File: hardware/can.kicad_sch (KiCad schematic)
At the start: 8 parts, among them U6 ATA6561

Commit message: Assign footprints to symbols
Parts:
- FB1, FB2: value 60R@100MHz -> 50mΩ@100MHz; footprint Inductor_SMD:L_0603_1608Metric -> Inductor_SMD:L_1206_3216Metric
- JP1: footprint Connector_PinHeader_2.54mm:PinHeader_1x02_P2.54mm_Vertical -> Connector_PinHeader_2.54mm:PinHeader_1x02_P2.54mm_Vertical_SMD_Pin1Left
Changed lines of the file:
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@@
       (effects (font (size 1.27 1.27)) (justify left))
     )
-    (property "Value" "60R@100MHz" (id 1) (at 99.06 96.52 0)
-      (effects (font (size 1.27 1.27)) (justify left))
-    )
-    (property "Footprint" "Inductor_SMD:L_0603_1608Metric" (id 2) (at 112.522 95.25 90)
+    (property "Value" "50mΩ@100MHz" (id 1) (at 96.52 96.52 0)
+      (effects (font (size 1.27 1.27)) (justify left))
+    )
+    (property "Footprint" "Inductor_SMD:L_1206_3216Metric" (id 2) (at 112.522 95.25 90)
       (effects (font (size 1.27 1.27)) hide)
     )
@@
       (effects (font (size 1.27 1.27)) (justify left))
     )
-    (property "Footprint" "Connector_PinHeader_2.54mm:PinHeader_1x02_P2.54mm_Vertical" (id 2) (at 194.31 92.71 0)
+    (property "Footprint" "Connector_PinHeader_2.54mm:PinHeader_1x02_P2.54mm_Vertical_SMD_Pin1Left" (id 2) (at 194.31 92.71 0)
       (effects (font (size 1.27 1.27)) hide)
     )
@@
       (effects (font (size 1.27 1.27)) (justify left))
     )
-    (property "Value" "60R@100MHz" (id 1) (at 129.54 81.153 0)
-      (effects (font (size 1.27 1.27)) (justify left))
-    )
-    (property "Footprint" "Inductor_SMD:L_0603_1608Metric" (id 2) (at 143.002 80.01 90)
-      (effects (font (size 1.27 1.27)) hide)
-    )
+    (property "Value" "50mΩ@100MHz" (id 1) (at 127 81.153 0)
+      (effects (font (size 1.27 1.27)) (justify left))
+    )
+    (property "Footprint" "Inductor_SMD:L_1206_3216Metric" (id 2) (at 143.002 80.01 90)
+      (effects (font (size 1.27 1.27)) hide)
+    )

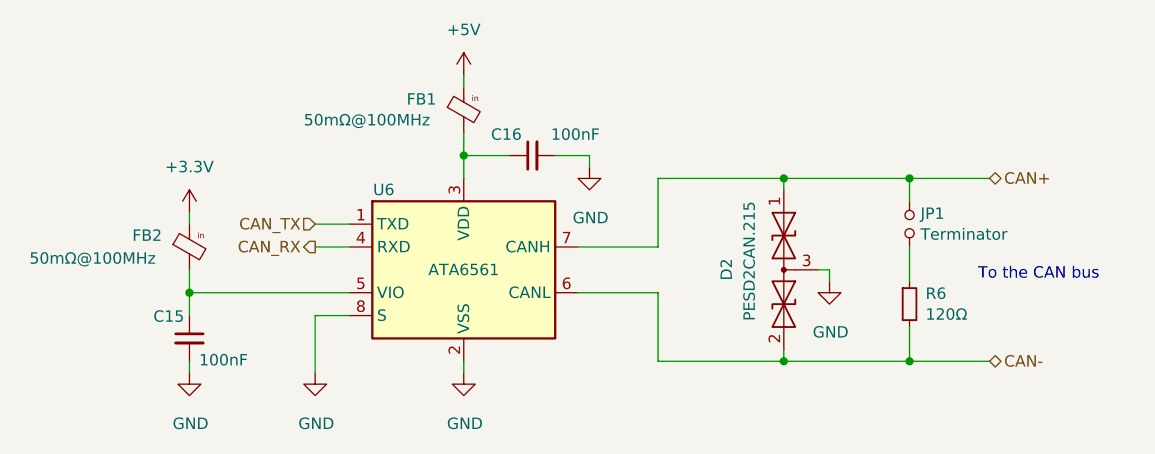
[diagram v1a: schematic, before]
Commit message: Use more efficient buck converter
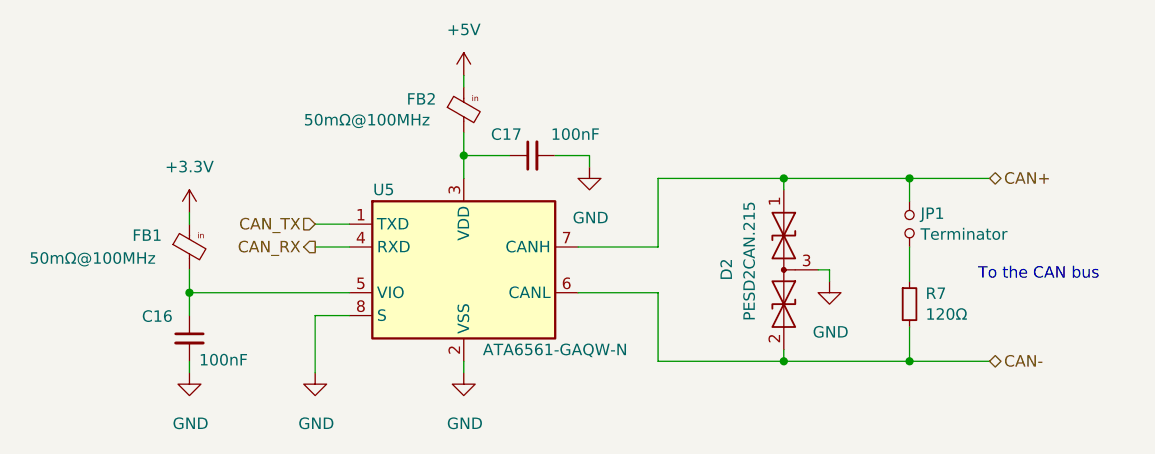
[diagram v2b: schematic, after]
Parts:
- U5: renamed from U6; value ATA6561 -> ATA6561-GAQW-N
- renumbered C15 to C16, C16 to C17, FB2 to FB1, FB1 to FB2, R6 to R7
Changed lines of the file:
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@@
   (symbol (lib_id "Local_Library:Ferrite_Bead_Small_PWR-PUTM_KICAD_SYMBOLS") (at 114.3 95.25 0) (unit 1)
     (in_bom yes) (on_board yes)
-    (property "Reference" "FB2" (id 0) (at 107.95 93.98 0)
+    (property "Reference" "FB1" (id 0) (at 107.95 93.98 0)
       (effects (font (size 1.27 1.27)) (justify left))
     )
@@
   (symbol (lib_id "power:GND") (at 128.27 109.22 0) (unit 1)
     (in_bom yes) (on_board yes)
-    (property "Reference" "#U0104" (id 0) (at 128.27 115.57 0)
+    (property "Reference" "#U02" (id 0) (at 128.27 115.57 0)
       (effects (font (size 1.27 1.27)) hide)
     )
@@
   (symbol (lib_id "power:GND") (at 185.42 99.06 0) (unit 1)
     (in_bom yes) (on_board yes)
-    (property "Reference" "#U0106" (id 0) (at 185.42 105.41 0)
+    (property "Reference" "#U05" (id 0) (at 185.42 105.41 0)
       (effects (font (size 1.27 1.27)) hide)
     )
@@
   (symbol (lib_id "power:GND") (at 144.78 109.22 0) (unit 1)
     (in_bom yes) (on_board yes)
-    (property "Reference" "#U0105" (id 0) (at 144.78 115.57 0)
+    (property "Reference" "#U03" (id 0) (at 144.78 115.57 0)
       (effects (font (size 1.27 1.27)) hide)
     )
@@
   (symbol (lib_id "Device:C_Small") (at 114.3 105.41 0) (unit 1)
     (in_bom yes) (on_board yes)
-    (property "Reference" "C15" (id 0) (at 110.2868 102.9716 0)
+    (property "Reference" "C16" (id 0) (at 109.0168 102.9716 0)
       (effects (font (size 1.27 1.27)) (justify left))
     )
@@
   (symbol (lib_id "Device:C_Small") (at 152.4 85.09 90) (unit 1)
     (in_bom yes) (on_board yes)
-    (property "Reference" "C16" (id 0) (at 151.2316 82.7532 90)
+    (property "Reference" "C17" (id 0) (at 151.2316 82.7532 90)
       (effects (font (size 1.27 1.27)) (justify left))
     )
@@
   (symbol (lib_id "power:GND") (at 114.3 109.22 0) (unit 1)
     (in_bom yes) (on_board yes)
-    (property "Reference" "#U0103" (id 0) (at 114.3 115.57 0)
+    (property "Reference" "#U01" (id 0) (at 114.3 115.57 0)
       (effects (font (size 1.27 1.27)) hide)
     )
@@
   (symbol (lib_id "power:+5V") (at 144.78 76.2 0) (unit 1)
     (in_bom yes) (on_board yes)
-    (property "Reference" "#PWR019" (id 0) (at 144.78 80.01 0)
+    (property "Reference" "#PWR024" (id 0) (at 144.78 80.01 0)
       (effects (font (size 1.27 1.27)) hide)
     )
@@
   (symbol (lib_id "power:GND") (at 158.75 86.36 0) (unit 1)
     (in_bom yes) (on_board yes)
-    (property "Reference" "#U0107" (id 0) (at 158.75 92.71 0)
+    (property "Reference" "#U04" (id 0) (at 158.75 92.71 0)
       (effects (font (size 1.27 1.27)) hide)
     )
@@
   (symbol (lib_id "power:+3.3V") (at 114.3 91.44 0) (unit 1)
     (in_bom yes) (on_board yes)
-    (property "Reference" "#PWR0102" (id 0) (at 114.3 95.25 0)
+    (property "Reference" "#PWR023" (id 0) (at 114.3 95.25 0)
       (effects (font (size 1.27 1.27)) hide)
     )
@@
   (symbol (lib_id "Device:R_Small") (at 194.31 101.6 0) (unit 1)
     (in_bom yes) (on_board yes)
-    (property "Reference" "R6" (id 0) (at 196.088 100.4316 0)
+    (property "Reference" "R7" (id 0) (at 196.088 100.4316 0)
       (effects (font (size 1.27 1.27)) (justify left))
     )
@@
   (symbol (lib_id "Interface_CAN_LIN:MCP2558FD-xSN") (at 144.78 97.79 0) (unit 1)
     (in_bom yes) (on_board yes)
-    (property "Reference" "U6" (id 0) (at 135.89 88.9 0))
-    (property "Value" "ATA6561" (id 1) (at 144.78 97.79 0))
+    (property "Reference" "U5" (id 0) (at 135.89 88.9 0))
+    (property "Value" "ATA6561-GAQW-N" (id 1) (at 154.94 106.68 0))
     (property "Footprint" "Package_SO:SOIC-8_3.9x4.9mm_P1.27mm" (id 2) (at 144.78 113.03 0)
       (effects (font (size 1.27 1.27)) hide)
@@
   (symbol (lib_id "Local_Library:Ferrite_Bead_Small_PWR-PUTM_KICAD_SYMBOLS") (at 144.78 80.01 0) (unit 1)
     (in_bom yes) (on_board yes)
-    (property "Reference" "FB1" (id 0) (at 138.43 78.8416 0)
-      (effects (font (size 1.27 1.27)) (justify left))
-    )
+    (property "Reference" "FB2" (id 0) (at 138.43 78.8416 0)
+      (effects (font (size 1.27 1.27)) (justify left))
+    )

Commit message: Arrange footprints
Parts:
- renumbered JP1 to J5
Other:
- note removed: "To the CAN bus"
- moved on the sheet: C16, FB1
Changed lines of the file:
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@@
   (title_block
     (title "CAN Transceiver")
-    (date "2022-12-04")
-    (rev "0.1.0")
+    (date "2022-12-10")
+    (rev "${REVISION}")
     (company "PUT Motorsport")
-    (comment 1 "Author: I. Kajdan")
+    (comment 3 "Reviewer:")
+    (comment 4 "Author: I. Kajdan")
   )
   (junction (at 180.34 107.95) (diameter 0) (color 0 0 0 0)
@@
   (junction (at 180.34 87.63) (diameter 0) (color 0 0 0 0)
   )
-  (junction (at 114.3 100.33) (diameter 0) (color 0 0 0 0)
+  (junction (at 113.03 100.33) (diameter 0) (color 0 0 0 0)
   )
   (wire (pts (xy 166.37 87.63) (xy 180.34 87.63))
@@
     (stroke (width 0) (type default) (color 0 0 0 0))
   )
-  (wire (pts (xy 114.3 100.33) (xy 114.3 97.79))
+  (wire (pts (xy 113.03 100.33) (xy 113.03 97.79))
     (stroke (width 0) (type default) (color 0 0 0 0))
   )
@@
     (stroke (width 0) (type default) (color 0 0 0 0))
   )
-  (wire (pts (xy 114.3 100.33) (xy 114.3 102.87))
+  (wire (pts (xy 113.03 100.33) (xy 113.03 102.87))
     (stroke (width 0) (type default) (color 0 0 0 0))
   )
@@
     (stroke (width 0) (type default) (color 0 0 0 0))
   )
-  (wire (pts (xy 114.3 100.33) (xy 132.08 100.33))
+  (wire (pts (xy 113.03 100.33) (xy 132.08 100.33))
     (stroke (width 0) (type default) (color 0 0 0 0))
   )
@@
     (stroke (width 0) (type default) (color 0 0 0 0))
   )
-  (wire (pts (xy 114.3 91.44) (xy 114.3 92.71))
+  (wire (pts (xy 113.03 91.44) (xy 113.03 92.71))
     (stroke (width 0) (type default) (color 0 0 0 0))
   )
@@
     (stroke (width 0) (type default) (color 0 0 0 0))
   )
-  (wire (pts (xy 114.3 109.22) (xy 114.3 107.95))
+  (wire (pts (xy 113.03 109.22) (xy 113.03 107.95))
     (stroke (width 0) (type default) (color 0 0 0 0))
   )
@@
   (wire (pts (xy 128.27 102.87) (xy 132.08 102.87))
     (stroke (width 0) (type default) (color 0 0 0 0))
-  )
-  (text "To the CAN bus" (at 201.93 99.06 0)
-    (effects (font (size 1.27 1.27)) (justify left bottom))
   )
   (hierarchical_label "CAN+" (shape bidirectional) (at 203.2 87.63 0)
@@
     (effects (font (size 1.27 1.27)) (justify right))
   )
-  (symbol (lib_id "Local_Library:Ferrite_Bead_Small_PWR-PUTM_KICAD_SYMBOLS") (at 114.3 95.25 0) (unit 1)
-    (in_bom yes) (on_board yes)
-    (property "Reference" "FB1" (id 0) (at 107.95 93.98 0)
-      (effects (font (size 1.27 1.27)) (justify left))
-    )
-    (property "Value" "50mΩ@100MHz" (id 1) (at 96.52 96.52 0)
-      (effects (font (size 1.27 1.27)) (justify left))
-    )
-    (property "Footprint" "Inductor_SMD:L_1206_3216Metric" (id 2) (at 112.522 95.25 90)
-      (effects (font (size 1.27 1.27)) hide)
-    )
-    (property "Datasheet" "~" (id 3) (at 114.3 95.25 0)
+  (symbol (lib_id "Local_Library:Ferrite_Bead_Small_PWR-PUTM_KICAD_SYMBOLS") (at 113.03 95.25 0) (unit 1)
+    (in_bom yes) (on_board yes)
+    (property "Reference" "FB1" (id 0) (at 106.68 93.98 0)
+      (effects (font (size 1.27 1.27)) (justify left))
+    )
+    (property "Value" "50mΩ@100MHz" (id 1) (at 95.25 96.52 0)
+      (effects (font (size 1.27 1.27)) (justify left))
+    )
+    (property "Footprint" "Inductor_SMD:L_1206_3216Metric" (id 2) (at 111.252 95.25 90)
+      (effects (font (size 1.27 1.27)) hide)
+    )
+    (property "Datasheet" "~" (id 3) (at 113.03 95.25 0)
       (effects (font (size 1.27 1.27)) hide)
     )
@@
     (pin "1")
   )
-  (symbol (lib_id "Device:C_Small") (at 114.3 105.41 0) (unit 1)
-    (in_bom yes) (on_board yes)
-    (property "Reference" "C16" (id 0) (at 109.0168 102.9716 0)
-      (effects (font (size 1.27 1.27)) (justify left))
-    )
-    (property "Value" "100nF" (id 1) (at 115.3668 107.823 0)
-      (effects (font (size 1.27 1.27)) (justify left))
-    )
-    (property "Footprint" "Capacitor_SMD:C_0603_1608Metric" (id 2) (at 114.3 105.41 0)
-      (effects (font (size 1.27 1.27)) hide)
-    )
-    (property "Datasheet" "~" (id 3) (at 114.3 105.41 0)
+  (symbol (lib_id "Device:C_Small") (at 113.03 105.41 0) (unit 1)
+    (in_bom yes) (on_board yes)
+    (property "Reference" "C16" (id 0) (at 107.7468 102.9716 0)
+      (effects (font (size 1.27 1.27)) (justify left))
+    )
+    (property "Value" "100nF" (id 1) (at 114.0968 107.823 0)
+      (effects (font (size 1.27 1.27)) (justify left))
+    )
+    (property "Footprint" "Capacitor_SMD:C_0603_1608Metric" (id 2) (at 113.03 105.41 0)
+      (effects (font (size 1.27 1.27)) hide)
+    )
+    (property "Datasheet" "~" (id 3) (at 113.03 105.41 0)
       (effects (font (size 1.27 1.27)) hide)
     )
@@
   (symbol (lib_id "Local_Library:Jumper_NO_Small-Device") (at 194.31 92.71 270) (unit 1)
     (in_bom yes) (on_board yes)
-    (property "Reference" "JP1" (id 0) (at 195.5292 91.5416 90)
+    (property "Reference" "J5" (id 0) (at 195.5292 91.5416 90)
       (effects (font (size 1.27 1.27)) (justify left))
     )
@@
     (pin "2")
   )
-  (symbol (lib_id "power:GND") (at 114.3 109.22 0) (unit 1)
-    (in_bom yes) (on_board yes)
-    (property "Reference" "#U01" (id 0) (at 114.3 115.57 0)
-      (effects (font (size 1.27 1.27)) hide)
-    )
-    (property "Value" "GND" (id 1) (at 114.427 114.8842 0))
-    (property "Footprint" "" (id 2) (at 114.3 109.22 0)
-      (effects (font (size 1.27 1.27)) hide)
-    )
-    (property "Datasheet" "" (id 3) (at 114.3 109.22 0)
+  (symbol (lib_id "power:GND") (at 113.03 109.22 0) (unit 1)
+    (in_bom yes) (on_board yes)
+    (property "Reference" "#U01" (id 0) (at 113.03 115.57 0)
+      (effects (font (size 1.27 1.27)) hide)
+    )
+    (property "Value" "GND" (id 1) (at 113.157 114.8842 0))
+    (property "Footprint" "" (id 2) (at 113.03 109.22 0)
+      (effects (font (size 1.27 1.27)) hide)
+    )
+    (property "Datasheet" "" (id 3) (at 113.03 109.22 0)
       (effects (font (size 1.27 1.27)) hide)
     )
@@
     (pin "1")
   )
-  (symbol (lib_id "power:+3.3V") (at 114.3 91.44 0) (unit 1)
-    (in_bom yes) (on_board yes)
-    (property "Reference" "#PWR023" (id 0) (at 114.3 95.25 0)
-      (effects (font (size 1.27 1.27)) hide)
-    )
-    (property "Value" "+3.3V" (id 1) (at 114.3 86.36 0))
-    (property "Footprint" "" (id 2) (at 114.3 91.44 0)
-      (effects (font (size 1.27 1.27)) hide)
-    )
-    (property "Datasheet" "" (id 3) (at 114.3 91.44 0)
-      (effects (font (size 1.27 1.27)) hide)
-    )
+  (symbol (lib_id "power:+3.3V") (at 113.03 91.44 0) (unit 1)
+    (in_bom yes) (on_board yes)
+    (property "Reference" "#PWR023" (id 0) (at 113.03 95.25 0)
+      (effects (font (size 1.27 1.27)) hide)
+    )
+    (property "Value" "+3.3V" (id 1) (at 113.03 86.36 0))
+    (property "Footprint" "" (id 2) (at 113.03 91.44 0)
+      (effects (font (size 1.27 1.27)) hide)
+    )
+    (property "Datasheet" "" (id 3) (at 113.03 91.44 0)
+      (effects (font (size 1.27 1.27)) hide)
+    )

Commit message: Apply PUTM branding
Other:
- company: PUT Motorsport -> Author: I. Kajdan
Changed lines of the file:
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@@
   (title_block
     (title "CAN Transceiver")
-    (date "2022-12-10")
+    (date "2022-12-11")
     (rev "${REVISION}")
-    (company "PUT Motorsport")
-    (comment 3 "Reviewer:")
-    (comment 4 "Author: I. Kajdan")
+    (company "Author: I. Kajdan")
   )
   (junction (at 180.34 107.95) (diameter 0) (color 0 0 0 0)

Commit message: Miscellaneous changes
- Use THT connectors
- Adjust ADC circuit according to the datasheet
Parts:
- J5: footprint Connector_PinHeader_2.54mm:PinHeader_1x02_P2.54mm_Vertical_SMD_Pin1Left -> Connector_PinHeader_2.54mm:PinHeader_1x02_P2.54mm_Vertical
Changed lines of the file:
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@@
       (effects (font (size 1.27 1.27)) (justify left))
     )
-    (property "Footprint" "Connector_PinHeader_2.54mm:PinHeader_1x02_P2.54mm_Vertical_SMD_Pin1Left" (id 2) (at 194.31 92.71 0)
+    (property "Footprint" "Connector_PinHeader_2.54mm:PinHeader_1x02_P2.54mm_Vertical" (id 2) (at 194.31 92.71 0)
       (effects (font (size 1.27 1.27)) hide)
     )

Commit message: Release v1.0.0
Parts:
- renumbered C17 to C31, C16 to C32, FB2 to FB1, FB1 to FB2, R7 to R15, U5 to U7
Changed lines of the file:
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@@
   (title_block
     (title "CAN Transceiver")
-    (date "2022-12-22")
+    (date "2022-12-28")
     (rev "${REVISION}")
     (company "Author: I. Kajdan")
+    (comment 1 "Reviewer: M. Jaruga")
   )
   (junction (at 180.34 107.95) (diameter 0) (color 0 0 0 0)
@@
   (symbol (lib_id "Local_Library:Ferrite_Bead_Small_PWR-PUTM_KICAD_SYMBOLS") (at 113.03 95.25 0) (unit 1)
     (in_bom yes) (on_board yes)
-    (property "Reference" "FB1" (id 0) (at 106.68 93.98 0)
+    (property "Reference" "FB2" (id 0) (at 106.68 93.98 0)
       (effects (font (size 1.27 1.27)) (justify left))
     )
@@
   (symbol (lib_id "power:GND") (at 128.27 109.22 0) (unit 1)
     (in_bom yes) (on_board yes)
-    (property "Reference" "#U02" (id 0) (at 128.27 115.57 0)
+    (property "Reference" "#U04" (id 0) (at 128.27 115.57 0)
       (effects (font (size 1.27 1.27)) hide)
     )
@@
   (symbol (lib_id "power:GND") (at 185.42 99.06 0) (unit 1)
     (in_bom yes) (on_board yes)
-    (property "Reference" "#U05" (id 0) (at 185.42 105.41 0)
+    (property "Reference" "#U02" (id 0) (at 185.42 105.41 0)
       (effects (font (size 1.27 1.27)) hide)
     )
@@
   (symbol (lib_id "power:GND") (at 144.78 109.22 0) (unit 1)
     (in_bom yes) (on_board yes)
-    (property "Reference" "#U03" (id 0) (at 144.78 115.57 0)
+    (property "Reference" "#U05" (id 0) (at 144.78 115.57 0)
       (effects (font (size 1.27 1.27)) hide)
     )
@@
   (symbol (lib_id "Device:C_Small") (at 113.03 105.41 0) (unit 1)
     (in_bom yes) (on_board yes)
-    (property "Reference" "C16" (id 0) (at 107.7468 102.9716 0)
+    (property "Reference" "C32" (id 0) (at 107.7468 102.9716 0)
       (effects (font (size 1.27 1.27)) (justify left))
     )
@@
   (symbol (lib_id "Device:C_Small") (at 152.4 85.09 90) (unit 1)
     (in_bom yes) (on_board yes)
-    (property "Reference" "C17" (id 0) (at 151.2316 82.7532 90)
+    (property "Reference" "C31" (id 0) (at 151.2316 82.7532 90)
       (effects (font (size 1.27 1.27)) (justify left))
     )
@@
   (symbol (lib_id "power:GND") (at 113.03 109.22 0) (unit 1)
     (in_bom yes) (on_board yes)
-    (property "Reference" "#U01" (id 0) (at 113.03 115.57 0)
+    (property "Reference" "#U03" (id 0) (at 113.03 115.57 0)
       (effects (font (size 1.27 1.27)) hide)
     )
@@
   (symbol (lib_id "power:+5V") (at 144.78 76.2 0) (unit 1)
     (in_bom yes) (on_board yes)
-    (property "Reference" "#PWR024" (id 0) (at 144.78 80.01 0)
+    (property "Reference" "#PWR053" (id 0) (at 144.78 80.01 0)
       (effects (font (size 1.27 1.27)) hide)
     )
@@
   (symbol (lib_id "power:GND") (at 158.75 86.36 0) (unit 1)
     (in_bom yes) (on_board yes)
-    (property "Reference" "#U04" (id 0) (at 158.75 92.71 0)
+    (property "Reference" "#U01" (id 0) (at 158.75 92.71 0)
       (effects (font (size 1.27 1.27)) hide)
     )
@@
   (symbol (lib_id "power:+3.3V") (at 113.03 91.44 0) (unit 1)
     (in_bom yes) (on_board yes)
-    (property "Reference" "#PWR023" (id 0) (at 113.03 95.25 0)
+    (property "Reference" "#PWR054" (id 0) (at 113.03 95.25 0)
       (effects (font (size 1.27 1.27)) hide)
     )
@@
   (symbol (lib_id "Device:R_Small") (at 194.31 101.6 0) (unit 1)
     (in_bom yes) (on_board yes)
-    (property "Reference" "R7" (id 0) (at 196.088 100.4316 0)
+    (property "Reference" "R15" (id 0) (at 196.088 100.4316 0)
       (effects (font (size 1.27 1.27)) (justify left))
     )
@@
   (symbol (lib_id "Interface_CAN_LIN:MCP2558FD-xSN") (at 144.78 97.79 0) (unit 1)
     (in_bom yes) (on_board yes)
-    (property "Reference" "U5" (id 0) (at 135.89 88.9 0))
+    (property "Reference" "U7" (id 0) (at 135.89 88.9 0))
     (property "Value" "ATA6561-GAQW-N" (id 1) (at 154.94 106.68 0))
     (property "Footprint" "Package_SO:SOIC-8_3.9x4.9mm_P1.27mm" (id 2) (at 144.78 113.03 0)
@@
   (symbol (lib_id "Local_Library:Ferrite_Bead_Small_PWR-PUTM_KICAD_SYMBOLS") (at 144.78 80.01 0) (unit 1)
     (in_bom yes) (on_board yes)
-    (property "Reference" "FB2" (id 0) (at 138.43 78.8416 0)
-      (effects (font (size 1.27 1.27)) (justify left))
-    )
+    (property "Reference" "FB1" (id 0) (at 138.43 78.8416 0)
+      (effects (font (size 1.27 1.27)) (justify left))
+    )
